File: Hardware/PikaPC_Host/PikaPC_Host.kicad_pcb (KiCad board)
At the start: 4 copper layers, 101.6 x 101.6 mm, 244 parts, among them J1 DE9_Pins_MountingHoles, J2 DIN41612_03x32_C_Split, SW1 SW_Push, U1 PPC403GA, U10 IDT74ALVC164245, U11 IDT74ALVC164245, U12 IDT74ALVC164245, U2 ATF1508AS, U3 MCP120-315GI/TO, U4 GD75232N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

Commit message: Host card PCB layout
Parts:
- added C50: 10uF, Capacitor_SMD:CP_Elec_4x5.7, F.Cu at (81.3, 67.3)
- added C51: 10uF, Capacitor_SMD:CP_Elec_4x5.7, F.Cu at (171.4, 141.0)
- added C52: 10uF, Capacitor_SMD:CP_Elec_4x5.7, F.Cu at (174.0, 77.5)
- added C53: 10uF, Capacitor_SMD:CP_Elec_4x5.7, F.Cu at (161.3, 123.2)
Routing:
- net +3.3V: track 183.5 -> 187.0 mm, vias 50 -> 62
- net /Main Bus/~{Bus-ACK}: track 24.3 -> 23.2 mm
- net /Main Bus/~{Bus-BERR}: track 15.4 -> 16.1 mm
- net GND: track 228.7 -> 228.2 mm, vias 141 -> 165
- net +5V: vias 16 -> 28
- added copper zone on F.Cu, net +3.3V
- added copper zone on F.Cu, net +5V
- removed copper zone on In1.Cu, net GND

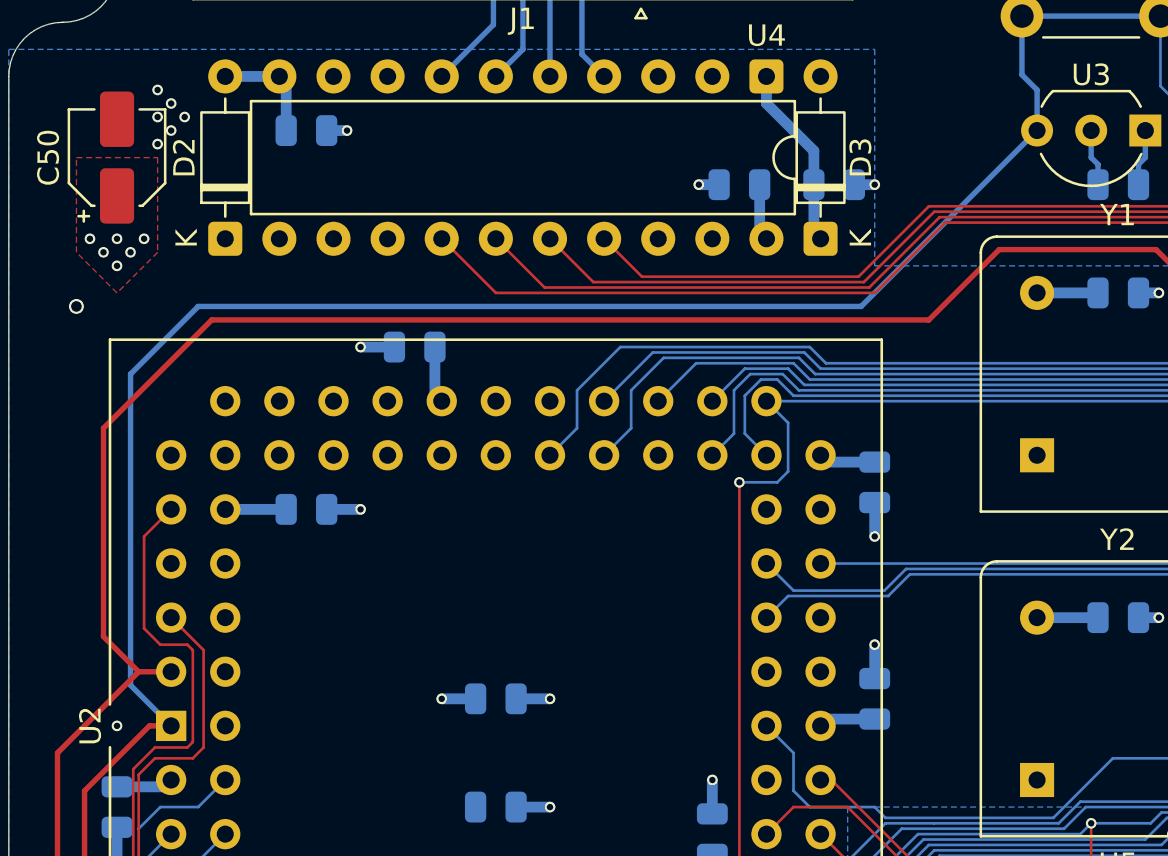
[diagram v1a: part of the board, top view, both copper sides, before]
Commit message: ViRGE card PCB layout
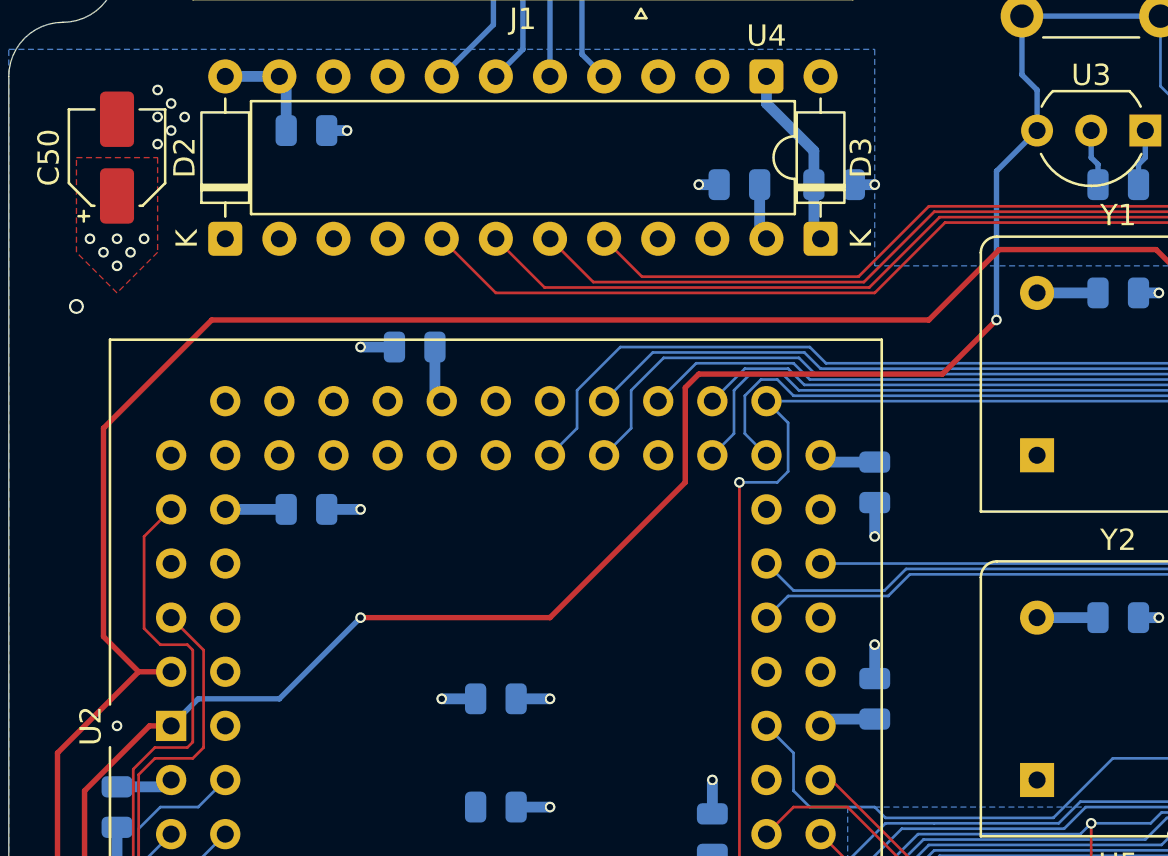
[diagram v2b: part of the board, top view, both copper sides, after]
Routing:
- net /~{Reset}: track 191.1 -> 185.4 mm, vias 2 -> 4
